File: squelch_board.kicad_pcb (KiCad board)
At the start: 2 copper layers, 50 x 50 mm, 104 parts, among them P1 PWR, P2 DISC., P3 OUT, P4 CONN_02X04, P5 CONN-10033526-N3212LF, P6 CONN_01X05, P7 LPF, P8 NOISE, P9 DISC., Q1 MMBT2222A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

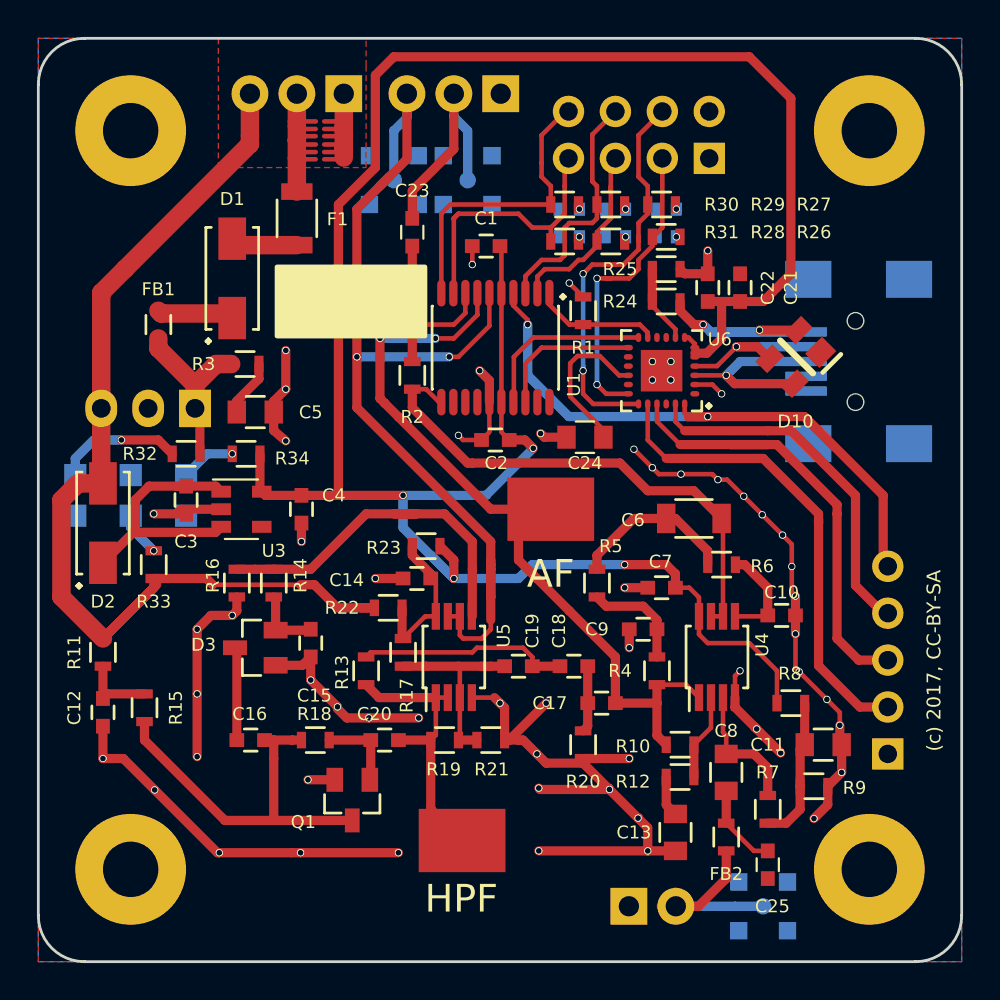
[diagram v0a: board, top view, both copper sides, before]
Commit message: Starting with rev 2.0 mods: Removing detector circuitry
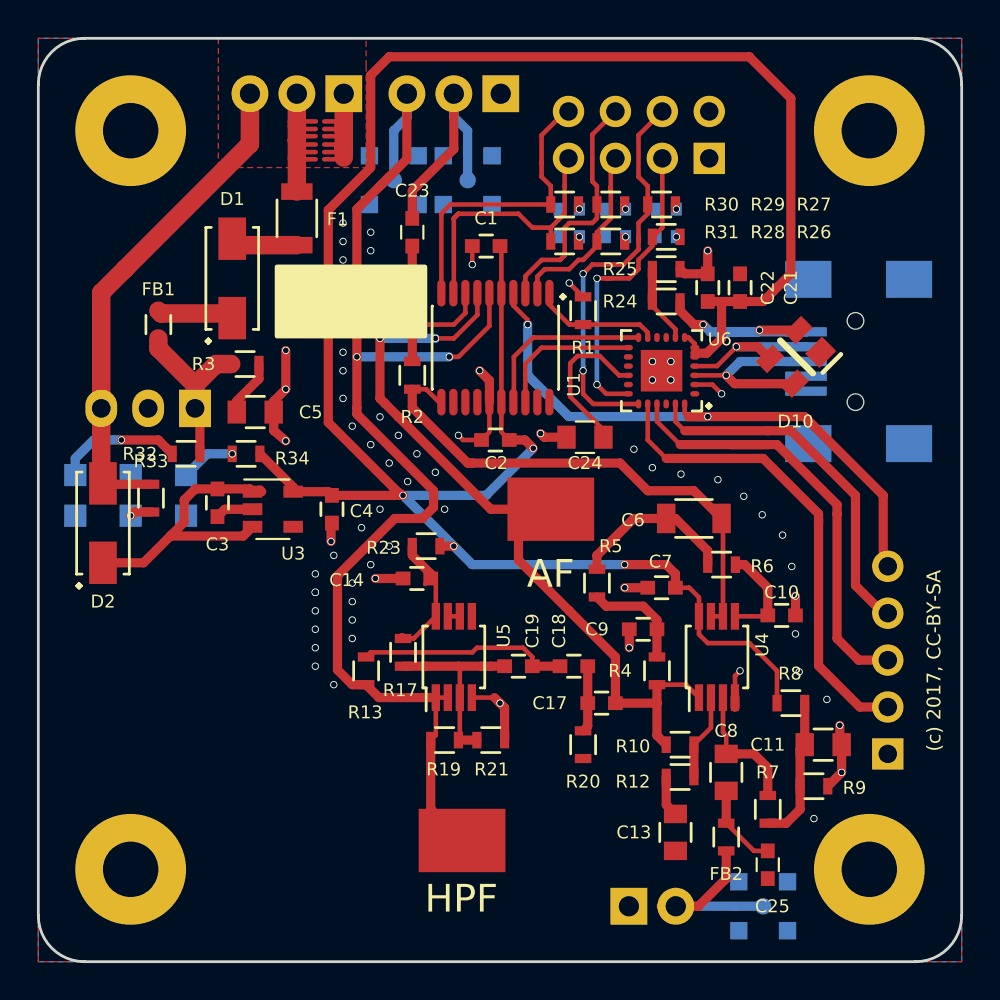
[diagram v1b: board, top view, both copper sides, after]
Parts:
- removed C12: 0.01u, Capacitors_SMD:C_0603
- removed C15: 0.0047u, Capacitors_SMD:C_0603
- removed C16: 0.1u, Capacitors_SMD:C_0603
- removed C20: 470p, Capacitors_SMD:C_0603
- removed D3: MMBD4148SE, smd-semi:SOT-23
- removed Q1: MMBT2222A, smd-semi:SOT-23
- removed R11: 100, Resistors_SMD:R_0603
- removed R14: 15k, Resistors_SMD:R_0603
- removed R15: 680, Resistors_SMD:R_0603
- removed R16: 100k, Resistors_SMD:R_0603
- removed R18: 470k, Resistors_SMD:R_0603
- removed R22: 0R, Resistors_SMD:R_0603
- P8: value NOISE -> HPF
- U3: value MIC5365 -> AP2202
- moved R33 3.60 mm to (121.1, 79.9), turned to 270 degrees
- moved C3 1.71 mm to (124.7, 80.2)
- moved U3 1.70 mm to (127.7, 80.5)
- moved C4 1.65 mm to (130.9, 80.5)
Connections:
- R13 pad 1: /HPF_OUT -> /NOISE
- R19 pad 2: /HPF_OUT -> /NOISE
- TP2 pad 1: /HPF_OUT -> /NOISE
- U5 pad 1: /HPF_OUT -> /NOISE
- U5 pad 2: /HPF_OUT -> /NOISE
- U5 pad 5: Net-(R14-Pad1) -> GND
- U5 pad 6: /NOISE -> Net-(U5-Pad6)
- U5 pad 7: /NOISE -> Net-(U5-Pad6)
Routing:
- net GND: track 143.6 -> 46.2 mm, vias 60 -> 77
- net /6V5: track 57.5 -> 27.2 mm
- net Net-(C16-Pad2): track 20.4 -> 0.00 mm
- net Net-(R14-Pad1): track 19.9 -> 0.00 mm
- net /HPF_OUT: track 15.0 -> 0.00 mm
- net /NOISE: track 54.9 -> 68.4 mm
- net Net-(C16-Pad1): track 5.04 -> 0.00 mm
- net Net-(C20-Pad1): track 4.42 -> 0.00 mm
- net Net-(C12-Pad1): track 4.10 -> 0.00 mm
- net Net-(C15-Pad1): track 3.76 -> 0.00 mm
- net /3V3: track 130.0 -> 126.7 mm
- net Net-(C3-Pad1): track 14.1 -> 15.6 mm
- net Net-(D12-Pad2): track 2.42 -> 1.18 mm
- net Net-(C14-Pad1): track 8.28 -> 7.10 mm
- net Net-(U5-Pad6): track 0.00 -> 0.65 mm

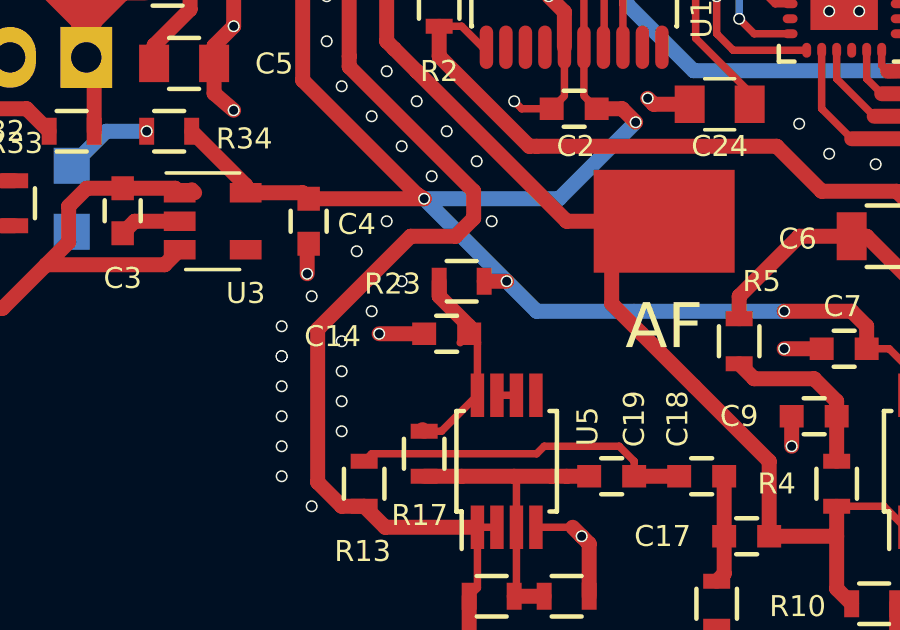
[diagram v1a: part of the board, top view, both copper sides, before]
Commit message: Removing R23 (selector for OPA rail voltage and potential ripple rejection)
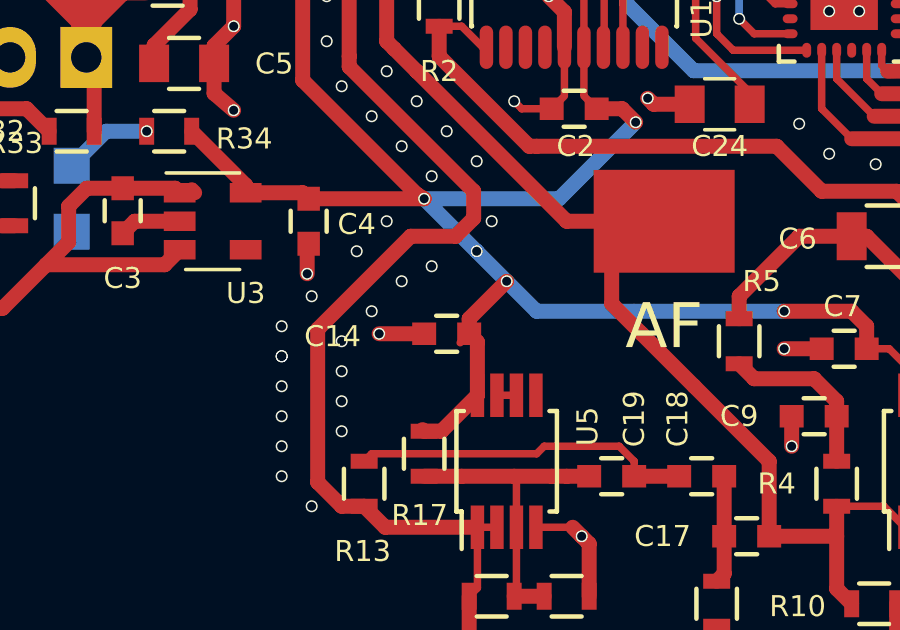
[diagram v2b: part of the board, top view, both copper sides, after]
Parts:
- removed R23: 0R, Resistors_SMD:R_0603
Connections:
- C14 pad 1: Net-(C14-Pad1) -> /3V3
- R17 pad 2: Net-(C14-Pad1) -> /3V3
- U5 pad 8: Net-(C14-Pad1) -> /3V3
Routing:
- net Net-(C14-Pad1): track 7.10 -> 0.00 mm
- net /3V3: track 126.7 -> 133.4 mm, vias 4 -> 5
- net GND: vias 77 -> 78

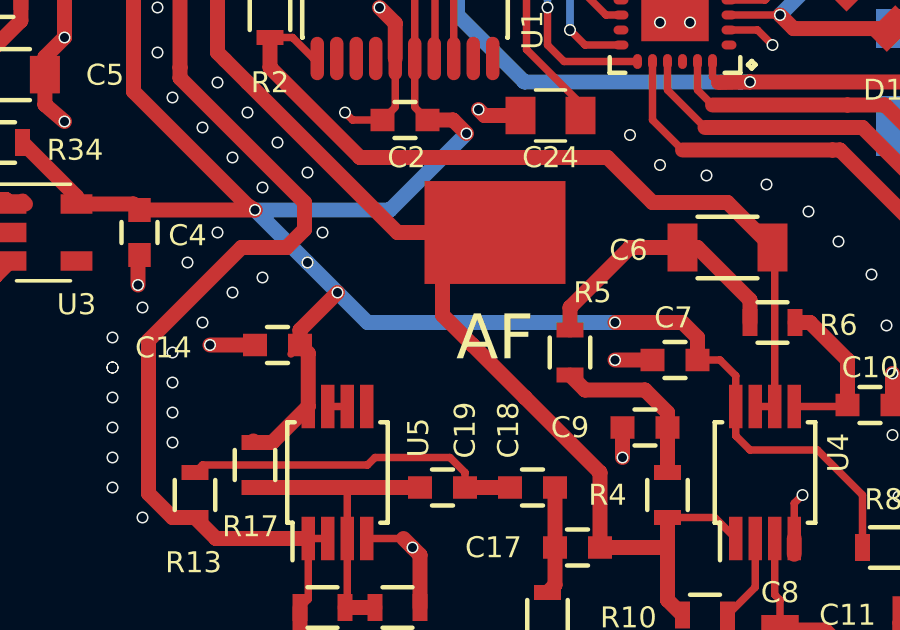
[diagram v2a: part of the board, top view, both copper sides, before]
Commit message: Adding fencing vias around AF_BUF track
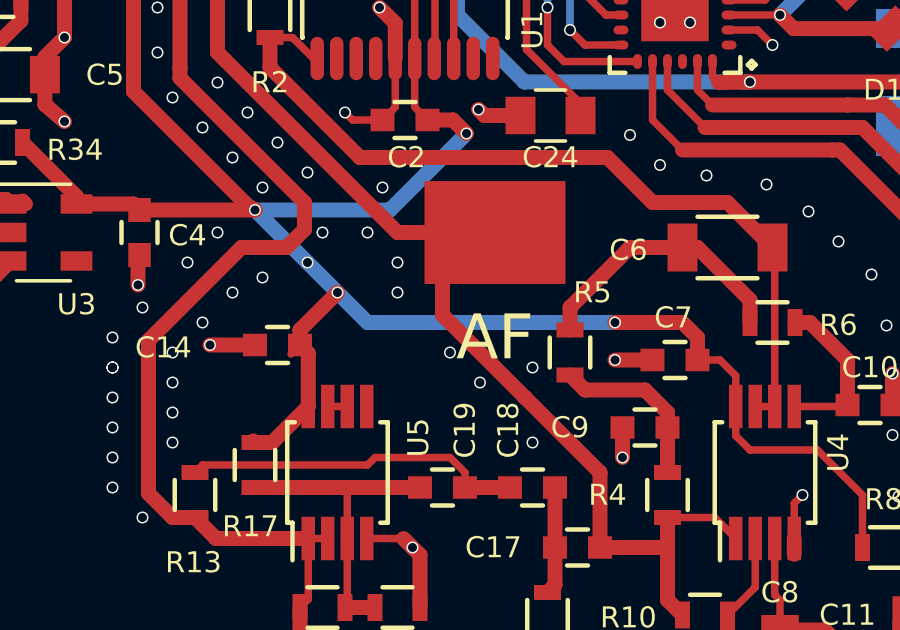
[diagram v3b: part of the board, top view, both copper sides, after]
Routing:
- net GND: vias 78 -> 86
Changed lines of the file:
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@@
     (thickness 1.6)
     (drawings 105)
-    (tracks 590)
+    (tracks 598)
     (zones 0)
     (modules 91)
@@
   (segment (start 140.25 93) (end 140.25 91.25) (width 0.5) (layer F.Cu) (net 1))
   (via (at 135 82) (size 0.4) (drill 0.3) (layers F.Cu B.Cu) (net 1))
+  (via (at 144 87.5) (size 0.4) (drill 0.3) (layers F.Cu B.Cu) (net 1))
+  (via (at 144 85) (size 0.4) (drill 0.3) (layers F.Cu B.Cu) (net 1))
+  (via (at 142.25 85.5) (size 0.4) (drill 0.3) (layers F.Cu B.Cu) (net 1))
+  (via (at 141.25 84.5) (size 0.4) (drill 0.3) (layers F.Cu B.Cu) (net 1))
+  (via (at 139.5 82.5) (size 0.4) (drill 0.3) (layers F.Cu B.Cu) (net 1))
+  (via (at 139.5 81.5) (size 0.4) (drill 0.3) (layers F.Cu B.Cu) (net 1))
+  (via (at 138.5 80.5) (size 0.4) (drill 0.3) (layers F.Cu B.Cu) (net 1))
+  (via (at 139 79) (size 0.4) (drill 0.3) (layers F.Cu B.Cu) (net 1))
   (segment (start 140.5 76.75) (end 141.35 76.75) (width 0.5) (layer F.Cu) (net 2))
   (segment (start 141.35 76.75) (end 141.8 77.2) (width 0.5) (layer F.Cu) (net 2))

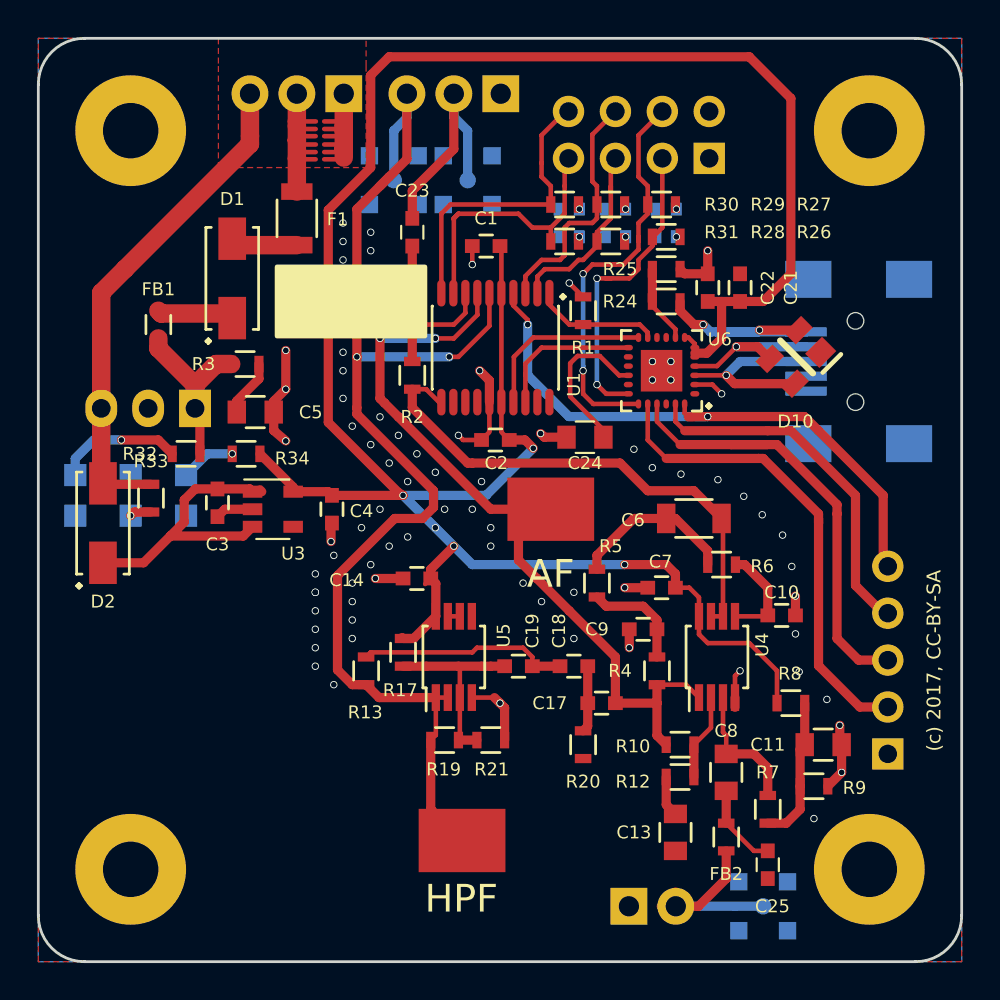
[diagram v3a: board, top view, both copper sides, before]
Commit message: Slight modification to avoid overlapping country-yard errors.
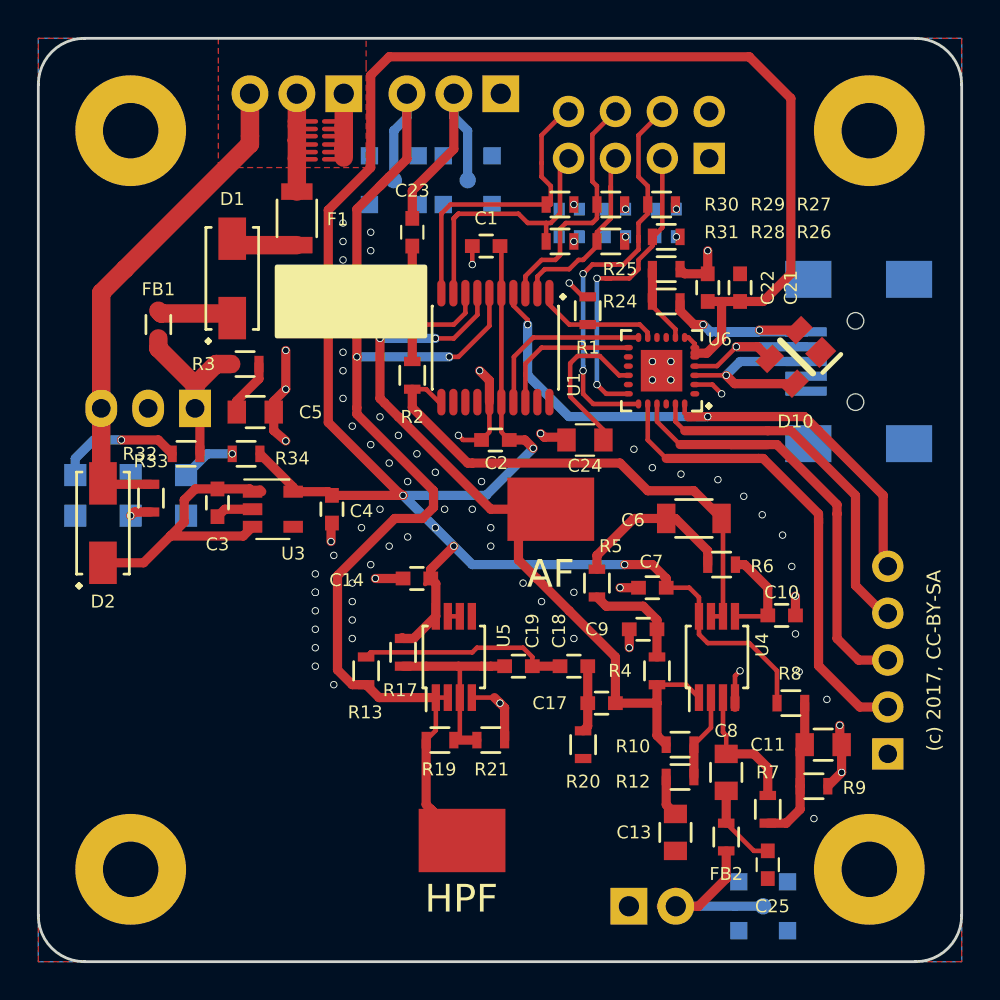
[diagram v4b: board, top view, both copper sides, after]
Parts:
- moved C7 0.50 mm to (148.2, 84.8)
- moved R1 0.25 mm to (144.8, 69.8)
- moved R19 0.25 mm to (136.8, 93.0)
- moved R30 0.25 mm to (143.2, 64.0)
- moved R31 0.25 mm to (143.2, 66.0)
- moved C24 0.15 mm to (144.6, 76.8)
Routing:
- net /NOISE: track 68.4 -> 71.0 mm
